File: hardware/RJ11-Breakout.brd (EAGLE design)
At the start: 15.2 x 20.3 mm, 5 parts

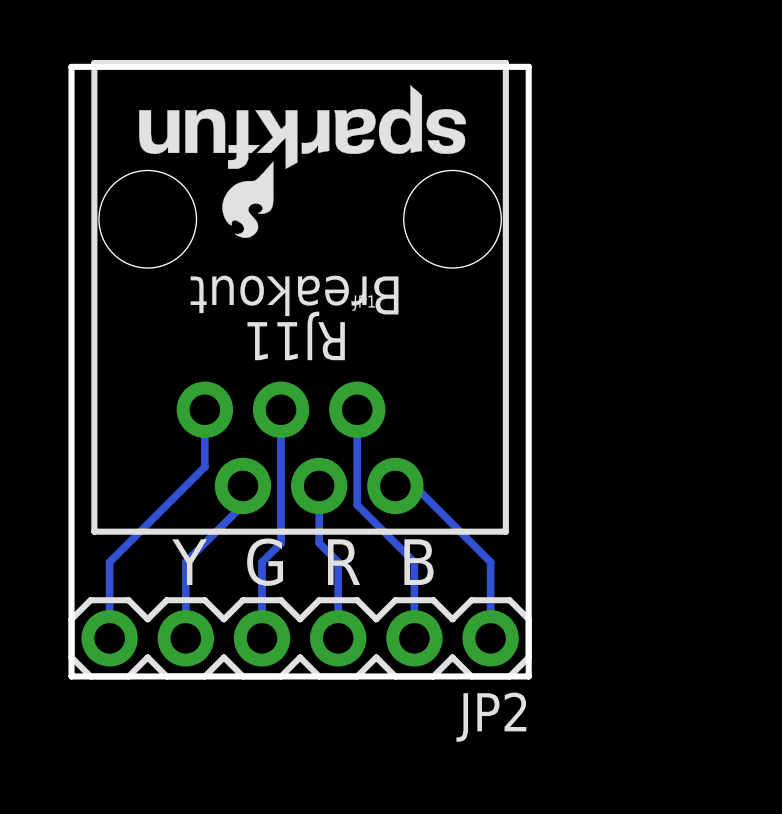
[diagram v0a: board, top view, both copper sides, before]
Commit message: Added gear, version, dimensions, mounting holes with v-score.
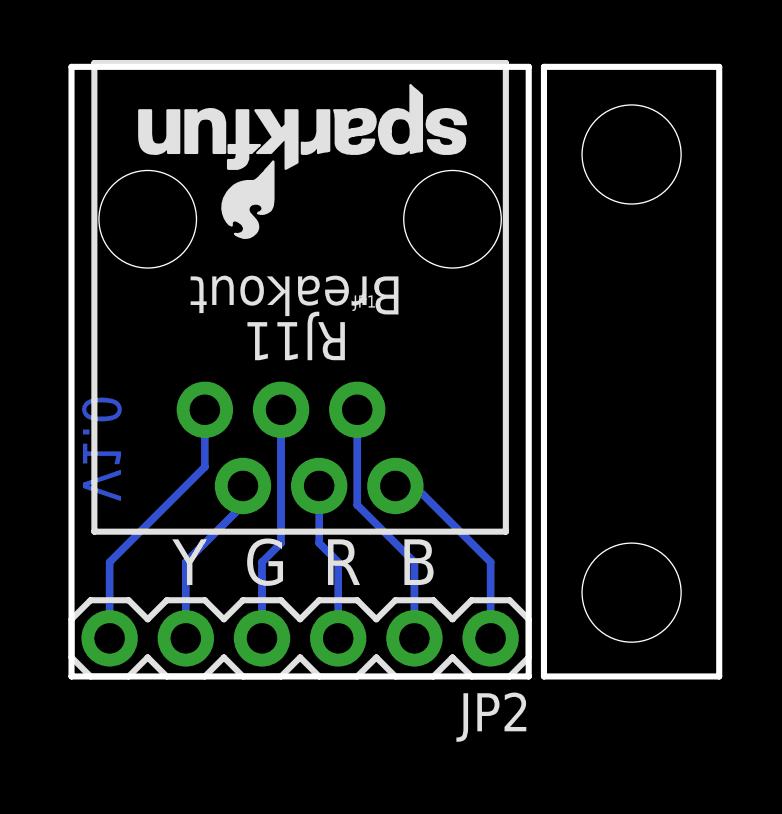
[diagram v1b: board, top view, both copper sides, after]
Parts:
- added H2, H4: STAND-OFF, SparkFun-Electromechanical:STAND-OFF
- added LOGO3: OSHW-LOGOMINI, SparkFun-Aesthetics:OSHW-LOGO-MINI
- FRAME2: value (none) -> FRAME-LETTER
- JP2: value (none) -> Pins
- moved FRAME2 3.81 mm to (-12.7, -12.7)
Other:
- board size 15.2 x 20.3 mm -> 21.6 x 20.3 mm
- board text added: "Don't cut v-score in production!"
- board text added: "V-score for the end user if they want to remove"
- board text added: "V1.0"
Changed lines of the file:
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@@
 <layer number="112" name="tSilk" color="7" fill="1" visible="no" active="yes"/>
 <layer number="113" name="IDFDebug" color="7" fill="1" visible="no" active="yes"/>
+<layer number="114" name="Badge_Outline" color="7" fill="1" visible="no" active="yes"/>
+<layer number="115" name="ReferenceISLANDS" color="7" fill="1" visible="no" active="yes"/>
 <layer number="116" name="Patch_BOT" color="9" fill="4" visible="no" active="yes"/>
+<layer number="118" name="Rect_Pads" color="7" fill="1" visible="no" active="yes"/>
 <layer number="121" name="_tsilk" color="7" fill="1" visible="no" active="yes"/>
 <layer number="122" name="_bsilk" color="7" fill="1" visible="no" active="yes"/>
@@
 <wire x1="0" y1="20.32" x2="15.24" y2="20.32" width="0.2032" layer="20"/>
 <wire x1="15.24" y1="20.32" x2="15.24" y2="0" width="0.2032" layer="20"/>
-<text x="17.78" y="-8.89" size="1.778" layer="51" font="vector" ratio="15">N. Seidle</text>
-<text x="13.97" y="-19.05" size="1.016" layer="47" font="vector" ratio="15">All dimensions are in inches.</text>
-<dimension x1="0" y1="0" x2="0" y2="30.48" x3="-3.81" y3="15.24" textsize="1.778" textratio="15" layer="47" unit="inch"/>
-<dimension x1="0" y1="30.48" x2="45.72" y2="30.48" x3="22.86" y3="40.64" textsize="1.778" textratio="15" layer="47" unit="inch"/>
-<dimension x1="1.27" y1="29.21" x2="44.45" y2="29.21" x3="22.86" y3="36.83" textsize="1.778" textratio="15" layer="47" unit="inch"/>
-<dimension x1="3.81" y1="1.27" x2="0" y2="1.27" x3="1.905" y3="-3.81" textsize="1.778" textratio="15" layer="47" unit="inch"/>
-<dimension x1="43.18" y1="15.24" x2="43.18" y2="0" x3="50.8" y3="7.62" textsize="1.778" textratio="15" layer="47" unit="inch"/>
+<text x="17.78" y="-12.7" size="1.778" layer="51" font="vector" ratio="15">N. Seidle</text>
+<text x="-3.81" y="-16.51" size="1.016" layer="47" font="vector" ratio="15">All dimensions are in inches.</text>
 <text x="7.493" y="11.176" size="1.27" layer="21" font="vector" ratio="15" rot="SR180" align="center">RJ11</text>
 <text x="7.493" y="12.7" size="1.27" layer="21" font="vector" ratio="15" rot="SR180" align="center">Breakout</text>
@@
 <text x="3.683" y="3.81" size="1.524" layer="22" font="vector" ratio="15" rot="SMR0" align="center">5</text>
 <text x="1.143" y="3.81" size="1.524" layer="22" font="vector" ratio="15" rot="SMR0" align="center">6</text>
+<text x="1.651" y="9.398" size="1.27" layer="16" font="vector" ratio="20" rot="MR270">V1.0</text>
+<dimension x1="15.24" y1="0" x2="15.24" y2="20.32" x3="33.02" y3="10.16" textsize="1.27" textratio="15" layer="47" unit="inch"/>
+<dimension x1="0.762" y1="20.447" x2="0.762" y2="23.368" x3="-2.54" y3="21.9075" textsize="1.27" textratio="15" layer="47" unit="inch"/>
+<dimension x1="0.762" y1="23.368" x2="14.478" y2="23.368" x3="7.62" y3="25.4" textsize="1.27" textratio="15" layer="47" unit="inch"/>
+<dimension x1="2.54" y1="15.24" x2="0" y2="15.24" x3="1.27" y3="21.59" textsize="1.27" textratio="15" layer="47" unit="inch"/>
+<dimension x1="3.81" y1="15.24" x2="3.81" y2="0" x3="-2.54" y3="7.62" textsize="1.27" textratio="15" layer="47" unit="inch"/>
+<wire x1="15.748" y1="20.32" x2="21.59" y2="20.32" width="0.2032" layer="20"/>
+<wire x1="21.59" y1="20.32" x2="21.59" y2="0" width="0.2032" layer="20"/>
+<wire x1="21.59" y1="0" x2="15.748" y2="0" width="0.2032" layer="20"/>
+<wire x1="15.748" y1="0" x2="15.748" y2="20.32" width="0.2032" layer="20"/>
+<text x="15.6972" y="21.4884" size="0.3048" layer="51" font="vector" ratio="15" align="top-left">V-score for the end user if they want to remove</text>
+<text x="15.7734" y="21.8948" size="1.016" layer="51" font="vector" ratio="15">Don't cut v-score in production!</text>
+<dimension x1="18.669" y1="2.794" x2="18.669" y2="0" x3="24.13" y3="1.397" textsize="1.27" textratio="15" layer="47" unit="inch"/>
+<dimension x1="18.669" y1="17.399" x2="18.669" y2="0" x3="27.94" y3="8.6995" textsize="1.27" textratio="15" layer="47" unit="inch"/>
+<dimension x1="0" y1="0" x2="15.24" y2="0" x3="7.62" y3="-3.81" textsize="1.27" textratio="15" layer="47" unit="inch"/>
 </plain>
 <attributes>
@@
 </class>
 </classes>
-<designrules name="default *">
-<description language="en">&lt;b&gt;EAGLE Design Rules&lt;/b&gt;
-&lt;p&gt;
-The default Design Rules have been set to cover
-a wide range of applications. Your particular design
-may have different requirements, so please make the
-necessary adjustments and save your customized
-design rules under a new name.</description>
+<designrules name="SparkFun-2-layer-STANDARD">
+<description language="en">&lt;b&gt;SparkFun 2 Layer Design Rule Checks - STANDARD/TIGHT/FAB-LIMIT&lt;/b&gt;
+&lt;p&gt;
+These rules have been curated by SparkFuns DFM commitee. After doing much research, communicating with our multiple fab houses, and getting quotes of various designs, we have compiled three DRU files.
+&lt;p&gt;
+&lt;b&gt;STANDARD:&lt;/b&gt; This is more of a &quot;best case scenario&quot; set of limitations. If your design has the space, and/or you have the time to work within these parameters, please do. Larger trace width and clearance makes for easier visual inspection of the PCB while troubleshooting (useful in production and to the end user). It also allows for better ability to hack a trace (if you are crazy enough to scrape away the mask and solder to a trace). Another thing to keep in mind is that more metal is just more robust.
+&lt;p&gt;
+&lt;b&gt;TIGHT:&lt;/b&gt; This is where cost comes into play. We have found that most fab houses begin to add extra charges when you go smaller than these specs. In some cases, going to less than 15 mil trace can increase the cost by 10%. (This is why we have set the min drill on this DRU to 15 mil) Same story for traces thinner than 7 mil. To avoid those extra charges, then stay within the rules of this DRU.
+&lt;p&gt;
+&lt;b&gt;FAB-LIMIT:&lt;/b&gt; These set of rules are at the very limit of most fab houses capabilities. You will pay more for these specs, and it should be used on designs that have a darned good reason to need 4 mil vias and 4 mil traces.
+&lt;p&gt;
+**NOTE Clearance, Distance, Sizes, and Restring are all set to different limits in each of these three DRU files. Please compare the files within the CAM job editor window of eagle to see all the numbers.
+&lt;p&gt;
+***NOTE, Please set your Net Classes to default (0mil for all settings), so that it won't effect the DRC when you run it with these settings.</description>
 <param name="layerSetup" value="(1*16)"/>
 <param name="mtCopper" value="0.035mm 0.035mm 0.035mm 0.035mm 0.035mm 0.035mm 0.035mm 0.035mm 0.035mm 0.035mm 0.035mm 0.035mm 0.035mm 0.035mm 0.035mm 0.035mm"/>
 <param name="mtIsolate" value="1.5mm 0.15mm 0.2mm 0.15mm 0.2mm 0.15mm 0.2mm 0.15mm 0.2mm 0.15mm 0.2mm 0.15mm 0.2mm 0.15mm 0.2mm"/>
-<param name="mdWireWire" value="8mil"/>
+<param name="mdWireWire" value="10mil"/>
 <param name="mdWirePad" value="8mil"/>
-<param name="mdWireVia" value="8mil"/>
+<param name="mdWireVia" value="10mil"/>
 <param name="mdPadPad" value="8mil"/>
-<param name="mdPadVia" value="8mil"/>
-<param name="mdViaVia" value="8mil"/>
+<param name="mdPadVia" value="10mil"/>
+<param name="mdViaVia" value="10mil"/>
 <param name="mdSmdPad" value="8mil"/>
 <param name="mdSmdVia" value="8mil"/>
@@
 <param name="mdViaViaSameLayer" value="8mil"/>
 <param name="mnLayersViaInSmd" value="2"/>
-<param name="mdCopperDimension" value="10mil"/>
+<param name="mdCopperDimension" value="8mil"/>
 <param name="mdDrill" value="8mil"/>
 <param name="mdSmdStop" value="0mil"/>
-<param name="msWidth" value="8mil"/>
+<param name="msWidth" value="10mil"/>
 <param name="msDrill" value="20mil"/>
 <param name="msMicroVia" value="9.99mm"/>
@@
 <param name="rvMicroViaOuter" value="0.25"/>
 <param name="rvMicroViaInner" value="0.25"/>
-<param name="rlMinPadTop" value="12mil"/>
+<param name="rlMinPadTop" value="10mil"/>
 <param name="rlMaxPadTop" value="20mil"/>
 <param name="rlMinPadInner" value="10mil"/>
 <param name="rlMaxPadInner" value="20mil"/>
-<param name="rlMinPadBottom" value="12mil"/>
+<param name="rlMinPadBottom" value="10mil"/>
 <param name="rlMaxPadBottom" value="20mil"/>
 <param name="rlMinViaOuter" value="10mil"/>
@@
 <attribute name="PROD_ID" value="CONN-08590" x="7.62" y="15.24" size="1.778" layer="27" font="vector" ratio="15" rot="R180" display="off"/>
 </element>
-<element name="FRAME2" library="SparkFun-Aesthetics" package="CREATIVE_COMMONS" value="" x="-12.7" y="-8.89">
-<attribute name="VERSION" value="v01" x="-12.7" y="-8.89" size="1.778" layer="27" font="vector" ratio="15" display="off"/>
-<attribute name="DESIGNER" value="NAME" x="-12.7" y="-8.89" size="1.778" layer="27" font="vector" ratio="15" display="off"/>
-</element>
-<element name="JP2" library="SparkFun-Connectors" package="1X06" value="" x="13.97" y="1.27" rot="R180">
+<element name="FRAME2" library="SparkFun-Aesthetics" package="CREATIVE_COMMONS" value="FRAME-LETTER" x="-12.7" y="-12.7"/>
+<element name="JP2" library="SparkFun-Connectors" package="1X06" value="Pins" x="13.97" y="1.27" rot="R180">
 <attribute name="PROD_ID" value="CONN-08437" x="13.97" y="1.27" size="1.778" layer="27" font="vector" ratio="15" rot="R180" display="off"/>
 </element>
 <element name="LOGO1" library="SparkFun-Aesthetics" package="SFE_LOGO_NAME_FLAME_.1" value="SFE_LOGO_NAME_FLAME.1_INCH" x="1.778" y="19.812" rot="MR180"/>
 <element name="LOGO2" library="SparkFun-Aesthetics" package="SFE_LOGO_NAME_FLAME_.1" value="SFE_LOGO_NAME_FLAME.1_INCH" x="13.589" y="19.812" rot="R180"/>
+<element name="LOGO3" library="SparkFun-Aesthetics" package="OSHW-LOGO-MINI" value="OSHW-LOGOMINI" x="12.7" y="8.89" rot="MR180"/>
+<element name="H2" library="SparkFun-Electromechanical" package="STAND-OFF" value="STAND-OFF" x="18.669" y="17.399"/>
+<element name="H4" library="SparkFun-Electromechanical" package="STAND-OFF" value="STAND-OFF" x="18.669" y="2.794"/>
 </elements>
 <signals>
@@
 </signal>
 </signals>
-<errors>
-</errors>
 </board>
 </drawing>

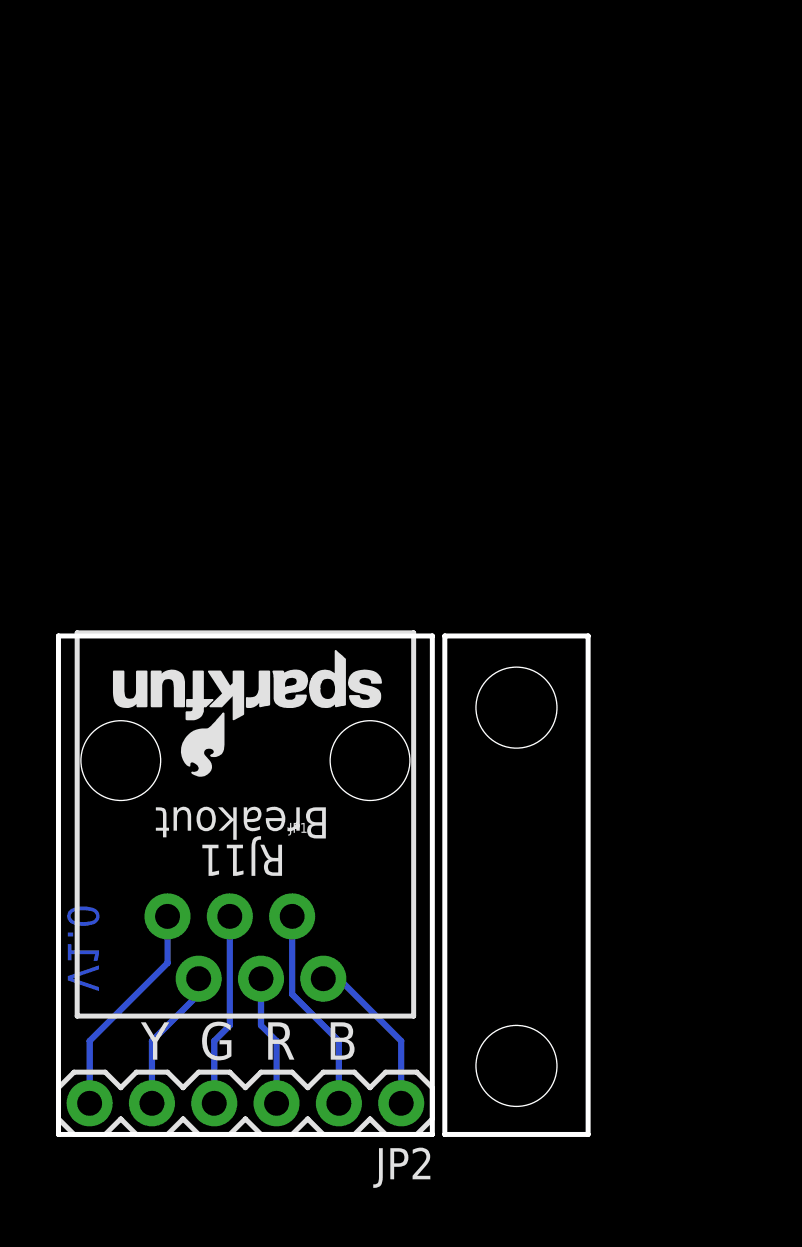
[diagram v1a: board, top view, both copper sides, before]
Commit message: Fixes to address issue 1
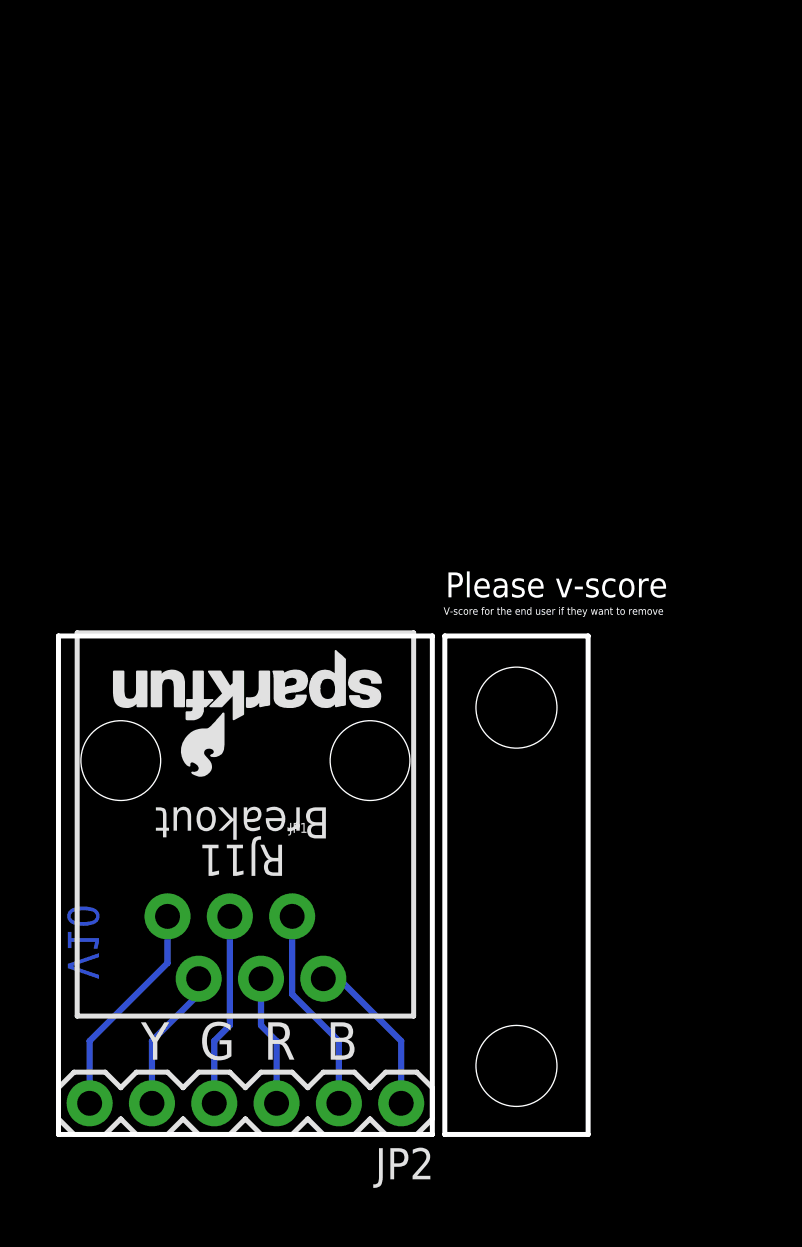
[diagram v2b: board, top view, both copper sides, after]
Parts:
- renumbered H2 to H3, H4 to H1
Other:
- board text added: "Please v-score"
- board text added: "V10"
- board text removed: "Don't cut v-score in production!"
- board text removed: "V1.0"
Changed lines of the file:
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@@
 <layer number="47" name="Measures" color="7" fill="1" visible="no" active="yes"/>
 <layer number="48" name="Document" color="7" fill="1" visible="no" active="yes"/>
-<layer number="49" name="Reference" color="7" fill="1" visible="yes" active="yes"/>
+<layer number="49" name="Reference" color="7" fill="1" visible="no" active="yes"/>
 <layer number="50" name="dxf" color="7" fill="1" visible="no" active="yes"/>
 <layer number="51" name="tDocu" color="6" fill="1" visible="yes" active="yes"/>
@@
 <text x="3.683" y="3.81" size="1.524" layer="22" font="vector" ratio="15" rot="SMR0" align="center">5</text>
 <text x="1.143" y="3.81" size="1.524" layer="22" font="vector" ratio="15" rot="SMR0" align="center">6</text>
-<text x="1.651" y="9.398" size="1.27" layer="16" font="vector" ratio="20" rot="MR270">V1.0</text>
+<text x="1.651" y="9.398" size="1.27" layer="16" font="vector" ratio="20" rot="MR270">V10</text>
 <dimension x1="15.24" y1="0" x2="15.24" y2="20.32" x3="33.02" y3="10.16" textsize="1.27" textratio="15" layer="47" unit="inch"/>
 <dimension x1="0.762" y1="20.447" x2="0.762" y2="23.368" x3="-2.54" y3="21.9075" textsize="1.27" textratio="15" layer="47" unit="inch"/>
@@
 <wire x1="21.59" y1="0" x2="15.748" y2="0" width="0.2032" layer="20"/>
 <wire x1="15.748" y1="0" x2="15.748" y2="20.32" width="0.2032" layer="20"/>
-<text x="15.6972" y="21.4884" size="0.3048" layer="51" font="vector" ratio="15" align="top-left">V-score for the end user if they want to remove</text>
-<text x="15.7734" y="21.8948" size="1.016" layer="51" font="vector" ratio="15">Don't cut v-score in production!</text>
+<text x="15.6972" y="21.4884" size="0.3048" layer="20" font="vector" ratio="15" align="top-left">V-score for the end user if they want to remove</text>
+<text x="15.7734" y="21.8948" size="1.016" layer="20" font="vector" ratio="15">Please v-score</text>
 <dimension x1="18.669" y1="2.794" x2="18.669" y2="0" x3="24.13" y3="1.397" textsize="1.27" textratio="15" layer="47" unit="inch"/>
 <dimension x1="18.669" y1="17.399" x2="18.669" y2="0" x3="27.94" y3="8.6995" textsize="1.27" textratio="15" layer="47" unit="inch"/>
@@
 <element name="LOGO2" library="SparkFun-Aesthetics" package="SFE_LOGO_NAME_FLAME_.1" value="SFE_LOGO_NAME_FLAME.1_INCH" x="13.589" y="19.812" rot="R180"/>
 <element name="LOGO3" library="SparkFun-Aesthetics" package="OSHW-LOGO-MINI" value="OSHW-LOGOMINI" x="12.7" y="8.89" rot="MR180"/>
-<element name="H2" library="SparkFun-Electromechanical" package="STAND-OFF" value="STAND-OFF" x="18.669" y="17.399"/>
-<element name="H4" library="SparkFun-Electromechanical" package="STAND-OFF" value="STAND-OFF" x="18.669" y="2.794"/>
+<element name="H1" library="SparkFun-Electromechanical" package="STAND-OFF" value="STAND-OFF" x="18.669" y="2.794"/>
+<element name="H3" library="SparkFun-Electromechanical" package="STAND-OFF" value="STAND-OFF" x="18.669" y="17.399"/>
 </elements>
 <signals>
